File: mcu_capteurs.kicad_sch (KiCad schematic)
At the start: 50 parts, among them J13 STLINK, SW1 435431019840, U5 STM32G474CEUx, Y1 16 MHz

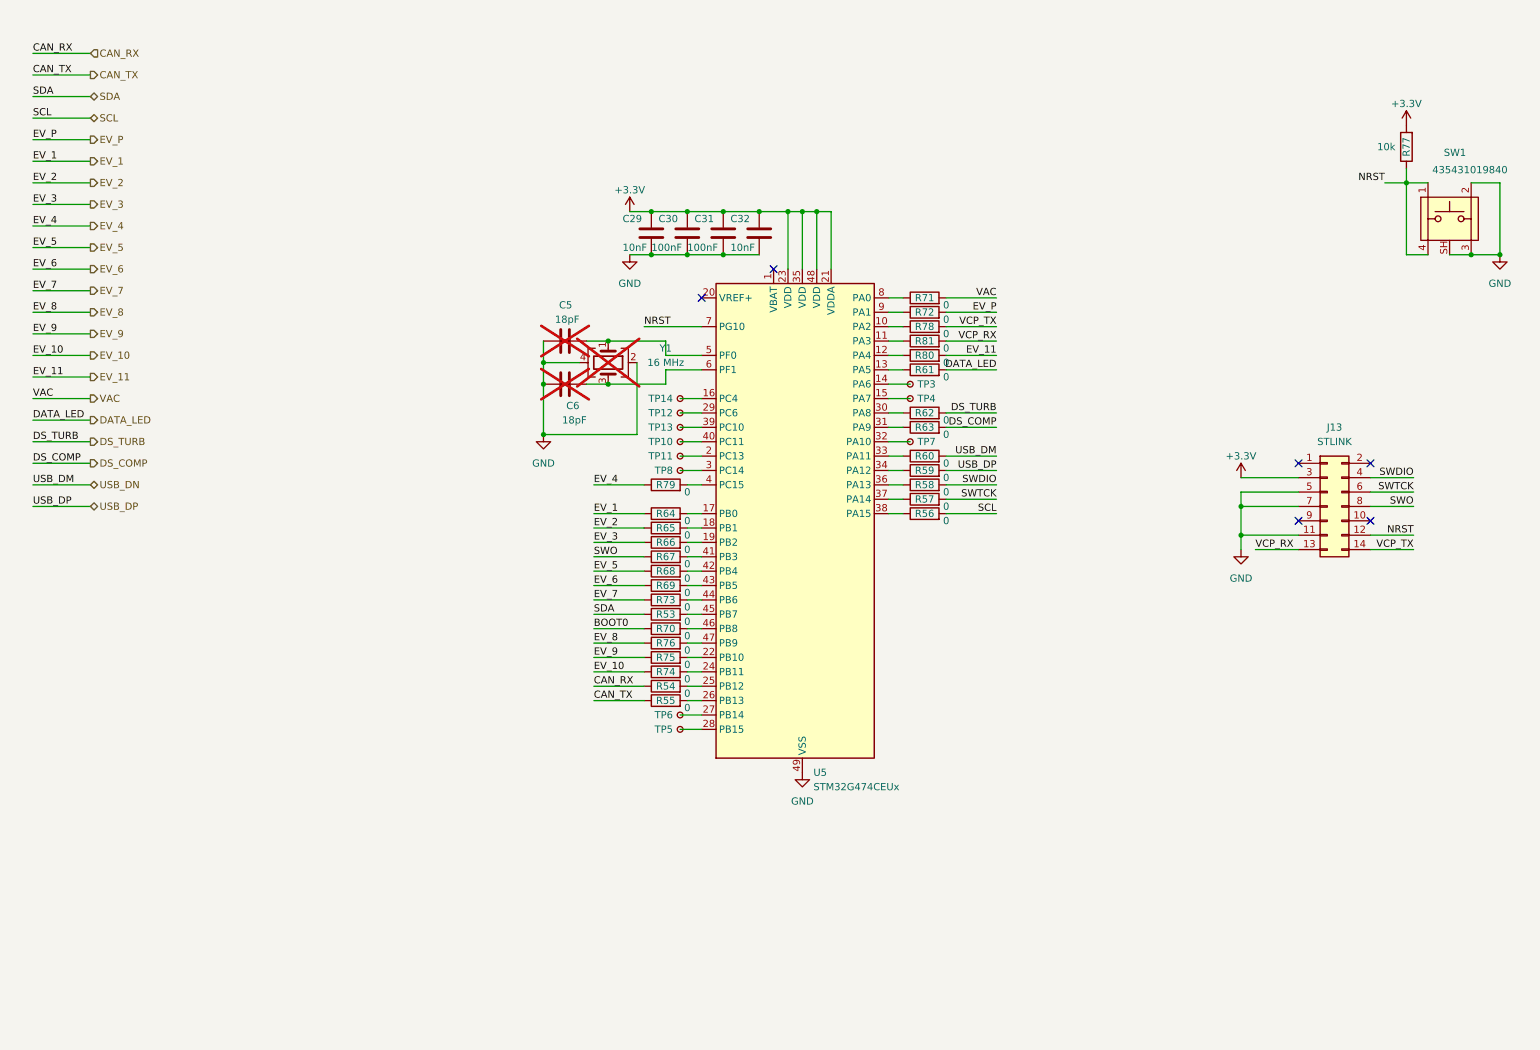
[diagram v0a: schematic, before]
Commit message: Simplification arborescence schema, correction duplicate designator TODO: connect floating signal on MCU sheet, update routing, split the board in two
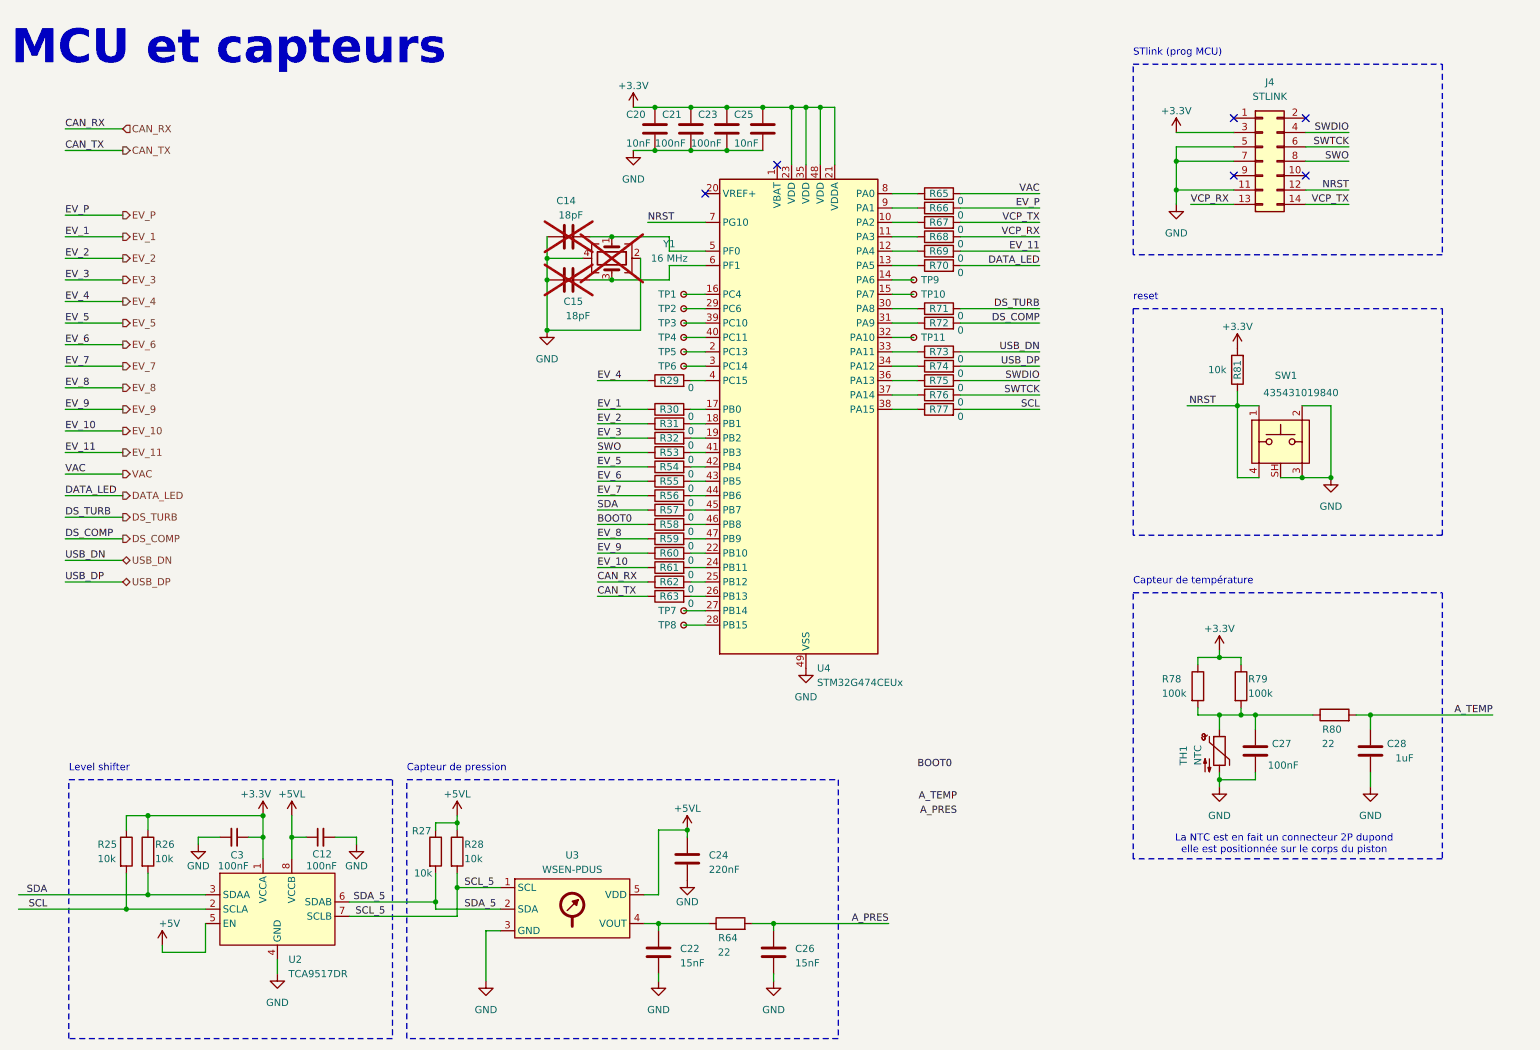
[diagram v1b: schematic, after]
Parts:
- removed C29, C32: 10nF, Capacitor_SMD:C_0603_1608Metric, symbol Device:C
- removed C30, C31: 100nF, Capacitor_SMD:C_0603_1608Metric, symbol Device:C
- removed C5, C6: 18pF, Capacitor_SMD:C_0603_1608Metric, symbol Device:C
- removed J13: STLINK, ConnectorsEvo:SAMTEC_FTSH-107-01-L-DV-K, symbol ConnectorsEvo:Conn_02x07_Odd_Even
- removed TP12, TP13, TP14: TestPoint_Small, TestPoint:TestPoint_Pad_D1.0mm, symbol Connector:TestPoint_Small
- removed U5: STM32G474CEUx, Package_DFN_QFN:QFN-48-1EP_7x7mm_P0.5mm_EP5.6x5.6mm, symbol MCU_ST_STM32G4:STM32G474CEUx
- added C12, C3: 100nF, Capacitor_SMD:C_0603_1608Metric, symbol Device:C_Small
- added C14, C15: 18pF, Capacitor_SMD:C_0603_1608Metric, symbol Device:C
- added C20, C25: 10nF, Capacitor_SMD:C_0603_1608Metric, symbol Device:C
- added C21, C23, C27: 100nF, Capacitor_SMD:C_0603_1608Metric, symbol Device:C
- added C22, C26: 15nF, Capacitor_SMD:C_0603_1608Metric, symbol Device:C
- added C24: 220nF, Capacitor_SMD:C_0603_1608Metric, symbol Device:C
- added C28: 1uF, Capacitor_SMD:C_0805_2012Metric, symbol Device:C
- added J4: STLINK, ConnectorsEvo:SAMTEC_FTSH-107-01-L-DV-K, symbol ConnectorsEvo:Conn_02x07_Odd_Even
- added R25, R26, R27, R28: 10k, Resistor_SMD:R_0603_1608Metric, symbol Device:R
- added R29, R30, R31, R32: 0, Resistor_SMD:R_0402_1005Metric, symbol Device:R
- added TH1: NTC, Connector_PinHeader_2.54mm:PinHeader_1x02_P2.54mm_Vertical, symbol Device:Thermistor_NTC
- added TP1, TP2, TP9: TestPoint_Small, TestPoint:TestPoint_Pad_D1.0mm, symbol Connector:TestPoint_Small
- added U2: TCA9517DR, Package_SO:SOIC-8_3.9x4.9mm_P1.27mm, symbol ComponentsEvo:TCA9517DR
- added U3: WSEN-PDUS, ComponentsEvo:WSEN-PDUS_2513130810X01, symbol ComponentsEvo:WSEN-PDUS
- added U4: STM32G474CEUx, Package_DFN_QFN:QFN-48-1EP_7x7mm_P0.5mm_EP5.6x5.6mm, symbol MCU_ST_STM32G4:STM32G474CEUx
- R64, R80: value 0 -> 22; footprint Resistor_SMD:R_0402_1005Metric -> Resistor_SMD:R_0603_1608Metric
- R77: value 10k -> 0
- R78, R79: value 0 -> 100k; footprint Resistor_SMD:R_0402_1005Metric -> Resistor_SMD:R_0603_1608Metric
- R81: value 0 -> 10k
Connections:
- net +3.3V: now also R78.1, R79.1, R81.2, C20.1, C21.1, C23.1, C25.1, C3.1, J4.3 (Pin_3), R25.1, R26.1, U2.1 (VCCA), U4.21 (VDDA), U4.23 (VDD), U4.35 (VDD), U4.48 (VDD); no longer R77.2
- net BOOT0: now also R58.1; no longer R70.1
- net CAN_RX: now also R62.1; no longer R54.1
- net CAN_TX: now also R63.1; no longer R55.1
- net DATA_LED: now also R70.2; no longer R61.2
- net DS_COMP: now also R72.2; no longer R63.2
- net DS_TURB: now also R71.2; no longer R62.2
- net EV_1: now also R30.1; no longer R64.1
- net EV_10: now also R61.1; no longer R74.1
- net EV_11: now also R69.2; no longer R80.2
- net EV_2: now also R31.1; no longer R65.1
- net EV_3: now also R32.1; no longer R66.1
- net EV_4: now also R29.1; no longer R79.1
- net EV_5: now also R54.1; no longer R68.1
- net EV_6: now also R55.1; no longer R69.1
- net EV_7: now also R56.1; no longer R73.1
- net EV_8: now also R59.1; no longer R76.1
- net EV_9: now also R60.1; no longer R75.1
- net EV_P: now also R66.2; no longer R72.2
- net GND: now also C12.2, C14.1, C15.1, C20.2, C21.2, C22.2, C23.2, C24.2, C25.2, C26.2, C27.1, C28.1, C3.2, J4.11 (Pin_11), J4.5 (Pin_5), J4.7 (Pin_7), TH1.2, U2.4 (GND), U3.3 (GND), U4.49 (VSS)
- net NRST: now also R81.1, J4.12 (Pin_12), U4.7 (PG10); no longer R77.1
- net SCL: now also R77.2, R25.2, U2.2 (SCLA); no longer R56.2
- net SDA: now also R57.1, R26.2, U2.3 (SDAA); no longer R53.1
- net SWDIO: now also R75.2, J4.4 (Pin_4); no longer R58.2
- net SWO: now also R53.1, J4.8 (Pin_8); no longer R67.1
- net SWTCK: now also R76.2, J4.6 (Pin_6); no longer R57.2
- net USB_DN: now also R73.2; no longer R60.2
- net USB_DP: now also R74.2; no longer R59.2
- net VAC: now also R65.2; no longer R71.2
- net VCP_RX: now also R68.2, J4.13 (Pin_13); no longer R81.2
- net VCP_TX: now also R67.2, J4.14 (Pin_14); no longer R78.2
- net at R55.2: now also U4.43 (PB5)
- net at Y1.1: now also C14.2, U4.5 (PF0)
- net at R53.2: now also U4.41 (PB3)
- net at R71.1: now also U4.30 (PA8)
- net at TP3.1: now also U4.39 (PC10)
- net at R54.2: now also U4.42 (PB4)
- net at R80.1: now also R78.2, R79.2, C27.2, TH1.1
- net at Y1.3: now also C15.2, U4.6 (PF1)
- net A_PRES: now reaches R64.2
- net A_PRES: now also C26.1
- net at TP7.1: now also U4.27 (PB14)
- net at TP10.1: now also U4.15 (PA7)
- net at TP8.1: now also U4.28 (PB15)
- net at TP4.1: now also U4.40 (PC11)
- net at TP11.1: now also U4.32 (PA10)
- net at TP6.1: now also U4.3 (PC14)
- net at TP5.1: now also U4.2 (PC13)
- net at R72.1: now also U4.31 (PA9)
- new net: TP2.1, U4.29 (PC6)
- new net: R32.2, U4.19 (PB2)
- new net: R76.1, U4.37 (PA14)
- new net: R77.1, U4.38 (PA15)
- new net: R29.2, U4.4 (PC15)
- new net: R67.1, U4.10 (PA2)
- new net: R66.1, U4.9 (PA1)
- new net: TP1.1, U4.16 (PC4)
- new net: R69.1, U4.12 (PA4)
- new net: TP9.1, U4.14 (PA6)
- new net: R56.2, U4.44 (PB6)
- new net: R63.2, U4.26 (PB13)
- new net: R70.1, U4.13 (PA5)
- new net: R57.2, U4.45 (PB7)
- new net: C22.1, R64.1, U3.4 (VOUT)
- new net: R61.2, U4.24 (PB11)
- new net: R68.1, U4.11 (PA3)
- new net: R30.2, U4.17 (PB0)
- new net: R31.2, U4.18 (PB1)
- new net: R60.2, U4.22 (PB10)
- new net: R62.2, U4.25 (PB12)
- new net: R73.1, U4.33 (PA11)
- new net: R74.1, U4.34 (PA12)
- new net: R75.1, U4.36 (PA13)
- new net: R58.2, U4.46 (PB8)
- new net: R59.2, U4.47 (PB9)
- new net: R65.1, U4.8 (PA0)
- new net +5V: U2.5 (EN)
- new net +5VL: C12.1, C24.1, R27.1, R28.1, U2.8 (VCCB), U3.5 (VDD)
- new net A_TEMP: C28.2, R80.2
- new net SCL_5: R28.2, U2.7 (SCLB), U3.1 (SCL)
- new net SDA_5: R27.2, U2.6 (SDAB), U3.2 (SDA)
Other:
- note added: "Capteur de pression"
- note added: "Capteur de température"
- note added: "La NTC est en fait un connecteur 2P dupond elle est positionnée sur le corps du piston"
- note added: "Level shifter"
- note added: "MCU et capteurs"
- note added: "STlink (prog MCU)"
- note added: "reset"
- company: (none) -> Équipe Goldorak
- title: (none) -> Carte pneumatique

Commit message: Correction de signaux non connectes, ajout de connecteur manquant, mise en forme du TOP
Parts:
- removed TP10, TP11, TP9: TestPoint_Small, TestPoint:TestPoint_Pad_D1.0mm, symbol Connector:TestPoint_Small
- added J15: BOOT0, symbol Connector:Conn_01x02_Pin
- added R82: 10k, Resistor_SMD:R_0603_1608Metric, symbol Device:R
- added R83, R84, R85, R86: 0, Resistor_SMD:R_0402_1005Metric, symbol Device:R
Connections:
- net +5VL: now also R86.1
- net A_PRES: now also R66.2
- net A_TEMP: now also R65.2
- net BOOT0: now also J15.1 (Pin_1)
- net DS_COMP: now also R71.2; no longer R72.2
- net DS_TURB: now also R85.2; no longer R71.2
- net EV_P: now also R83.2; no longer R66.2
- net GND: now also R82.2
- net VAC: now also R84.2; no longer R65.2
- net at R72.1: now also U4.32 (PA10); no longer U4.31 (PA9)
- net at U4.14 (PA6): now also R83.1
- net at U4.15 (PA7): now also R84.1
- net at U4.30 (PA8): now also R85.1; no longer R71.1
- net +5V: no longer names the net of U2.5 (EN)
- net +5V: now also R86.2
- new net: J15.2 (Pin_2), R82.1
- new net: R71.1, U4.31 (PA9)
- new net AU_STATUS: R72.2
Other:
- note added: "Verifier si AU_STATUS a besoin/ est bien sur une pin d'INT"
- moved on the sheet: R71, R72

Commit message: ajout d'une lib projet et synchro PCB
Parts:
- J15: footprint (none) -> Connector_PinHeader_2.54mm:PinHeader_1x02_P2.54mm_Vertical
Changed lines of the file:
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@@
 			)
 		)
-		(property "Footprint" ""
+		(property "Footprint" "Connector_PinHeader_2.54mm:PinHeader_1x02_P2.54mm_Vertical"
 			(at 102.87 103.505 0)
 			(effects

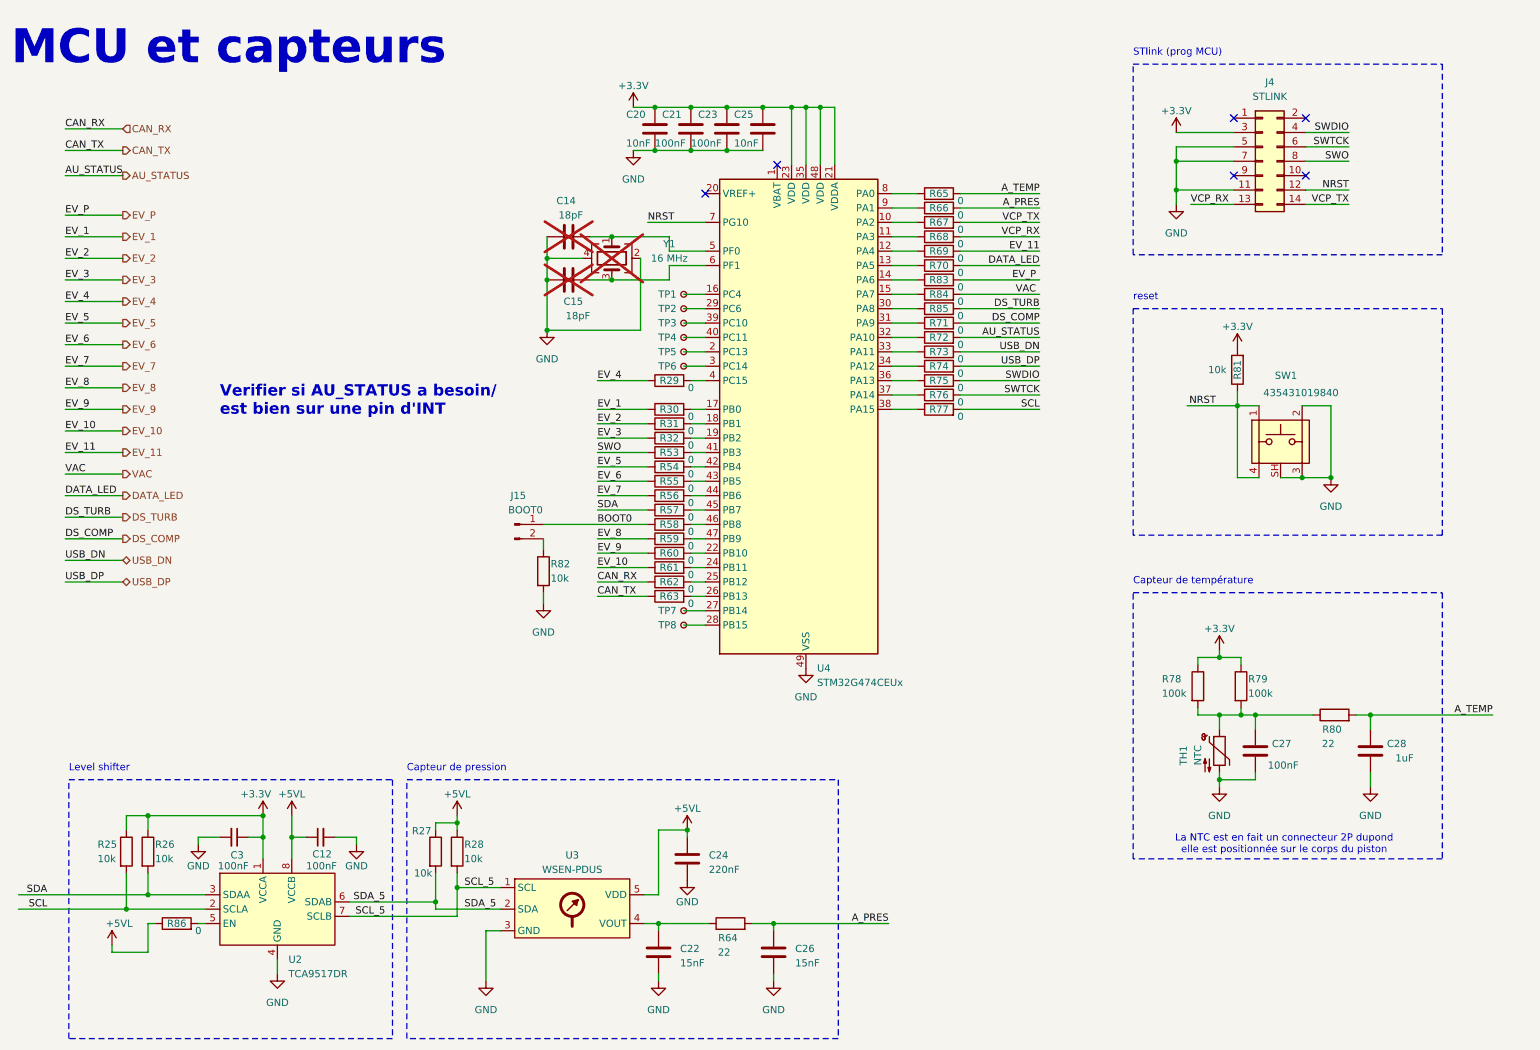
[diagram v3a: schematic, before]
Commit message: optimisation empreinte passif (TODO fp diode), TODO ajouter LED temoin diverse, groupement sur PCB des nouveaux composant
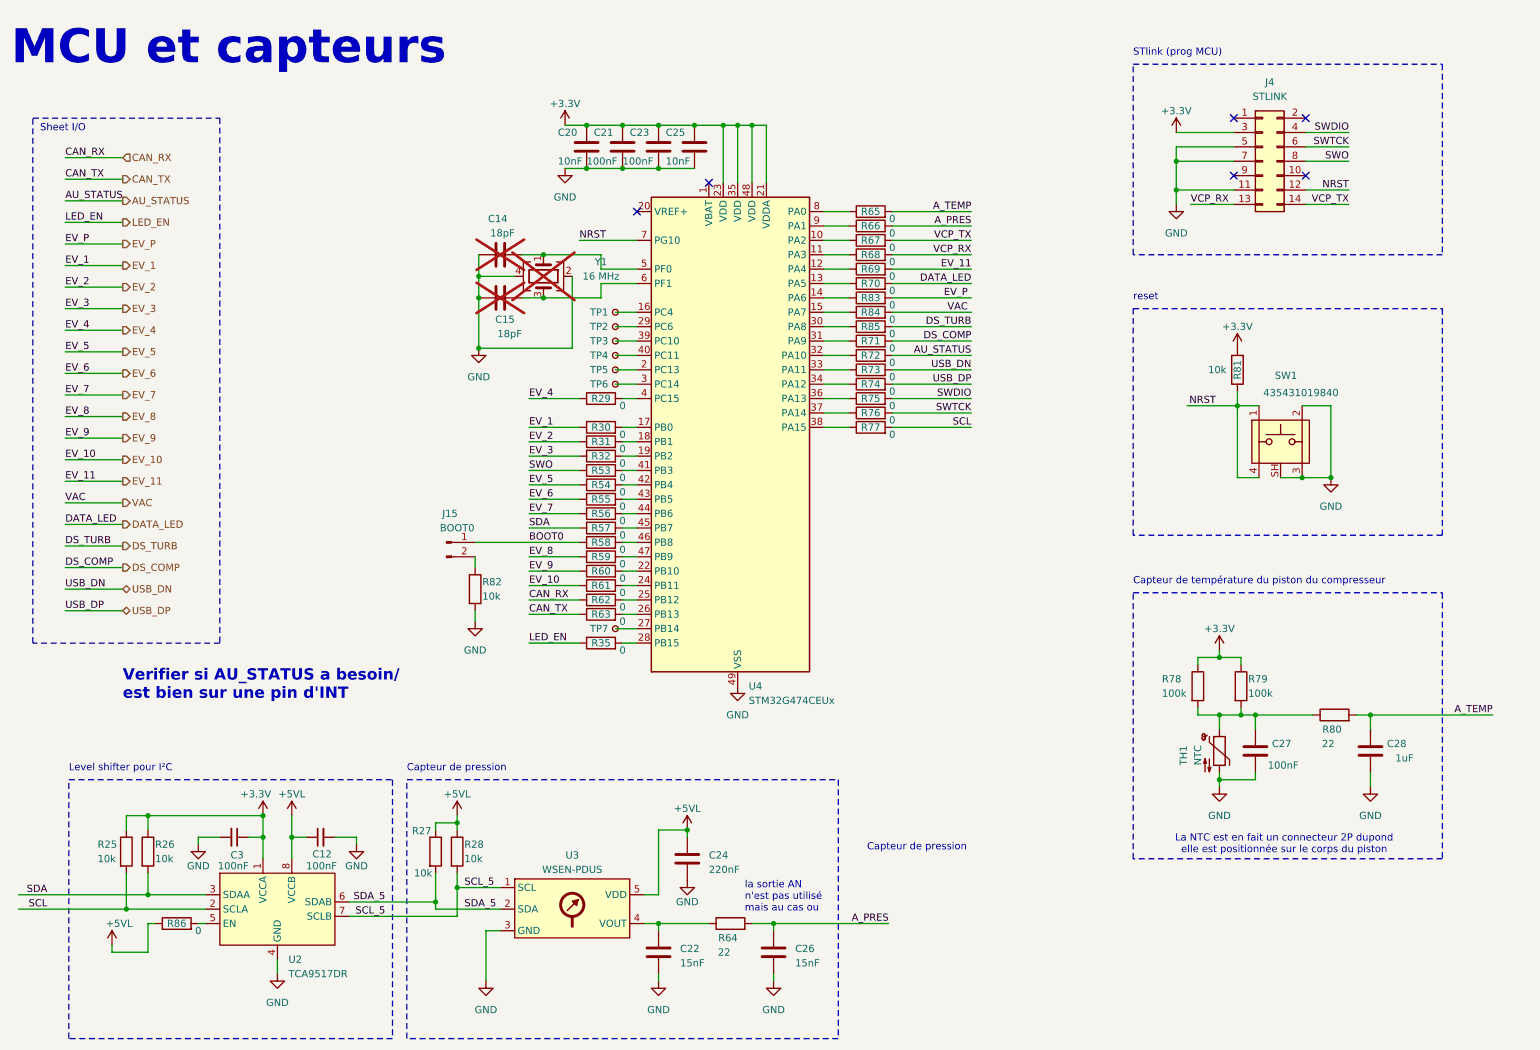
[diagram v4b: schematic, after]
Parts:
- removed TP8: TestPoint_Small, TestPoint:TestPoint_Pad_D1.0mm, symbol Connector:TestPoint_Small
- added R35: 0, Resistor_SMD:R_0402_1005Metric, symbol Device:R
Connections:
- net at U4.28 (PB15): now also R35.2
- new net LED_EN: R35.1
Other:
- note added: "Capteur de température du piston du compresseur"
- note added: "Level shifter pour I²C"
- note added: "Sheet I/O"
- note added: "la sortie AN n'est pas utilisé mais au cas ou"
- note removed: "Capteur de température"
- note removed: "Level shifter"
- moved on the sheet: C14, C15, C20, C21, C23, C25, J15, R29, R30, R31, R32, R53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
